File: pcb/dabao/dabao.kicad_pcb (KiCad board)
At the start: 2 copper layers, 127.4 x 114.6 mm, 74 parts, among them J1 Conn_01x05, J2 USB_C_Receptacle_USB2.0_16P, J3 Conn_01x04, J4 MagConn_01x04_Pin, J5 Conn_Battery, J7 Conn_01x04, J8 Display, SW1 SW_RESET, SW2 SW_POWER, U1 nice_nano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

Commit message: Add nets, tweak layout
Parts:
- moved REF** 4.97 mm to (168.5, 79.5)
- moved S3 4.45 mm to (104.5, 71.9)
- moved C1 4.45 mm to (135.7, 105.0)
- moved D2 4.45 mm to (102.7, 84.9)
- moved D3 4.45 mm to (107.1, 68.5)
- moved J8 4.45 mm to (206.8, 105.2)
- moved JP6 4.45 mm to (204.3, 123.7)
- moved JP8 4.45 mm to (204.3, 123.7)
- moved S18 4.45 mm to (184.3, 141.9)
- moved S8 4.45 mm to (141.1, 78.1)
- moved S12 4.45 mm to (162.3, 68.8)
- moved S7 4.45 mm to (136.7, 94.6)
- moved D13 4.45 mm to (172.8, 105.4)
- moved REF** 4.45 mm to (188.4, 128.5)
- moved S16 4.45 mm to (149.9, 122.0)
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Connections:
- J2 pad S1: unconnected-(J2-SHIELD-PadS1) -> GND
- U1 pad 29: unconnected-(U1-BAT+-Pad29) -> /BAT+
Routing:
- net /col_ring: track 180.7 -> 181.9 mm
- net /col_pinky: track 199.1 -> 199.9 mm
- net GND: vias 70 -> 73

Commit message: Add logo, update library path
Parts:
- added G***: LOGO, Library:takeout-text, F.Cu at (201.6, 142.7)
- added G***: LOGO, Library:takeout-logo, B.Cu at (200.0, 138.8)
- moved C1 2.22 mm to (134.9, 102.9)
- moved S15 2.22 mm to (178.1, 73.9)
- moved REF** 2.22 mm to (109.8, 82.4)
- moved S1 2.22 mm to (94.9, 102.6)
- moved S3 2.22 mm to (103.7, 69.8)
- moved D11 2.22 mm to (159.4, 79.8)
- moved J5 2.22 mm to (203.9, 110.2)
- moved JP3 2.22 mm to (208.4, 118.9)
- moved S12 2.22 mm to (161.4, 66.8)
- moved S17 2.22 mm to (167.6, 127.7)
- moved JP2 2.22 mm to (208.5, 121.7)
- moved JP5 2.22 mm to (203.5, 118.9)
- moved JP7 2.22 mm to (203.4, 118.9)
- moved R4 2.22 mm to (196.1, 88.2)
- moved REF** 2.22 mm to (167.6, 77.5)
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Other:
- board text added: "v1.0"
- board text removed: "打包 v1.0"

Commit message: Updates to models
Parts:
- moved REF** 20.6 mm to (188.1, 79.5)
- moved REF** 14.4 mm to (122.9, 49.0)
- moved REF** 2.29 mm to (188.6, 124.5)
- moved REF** 2.22 mm to (198.4, 151.9)
- moved D13 2.22 mm to (171.1, 101.3)
- moved D7 2.22 mm to (137.6, 87.1)
- moved JP11 2.22 mm to (198.1, 96.3)
- moved R8 2.22 mm to (130.3, 99.9)
- moved S16 2.22 mm to (148.2, 117.9)
- moved S17 2.22 mm to (166.7, 125.6)
- moved U2 2.22 mm to (185.9, 108.4)
- moved S1 2.22 mm to (94.0, 100.6)
- moved J7 2.22 mm to (197.7, 125.3)
- moved JP2 2.22 mm to (207.6, 119.6)
- moved JP5 2.22 mm to (202.6, 116.9)
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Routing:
- net GND: track 67.0 -> 64.6 mm, vias 73 -> 74
- net Net-(J5-Pin_2): track 115.3 -> 114.0 mm
- net /BAT+: track 68.7 -> 67.4 mm

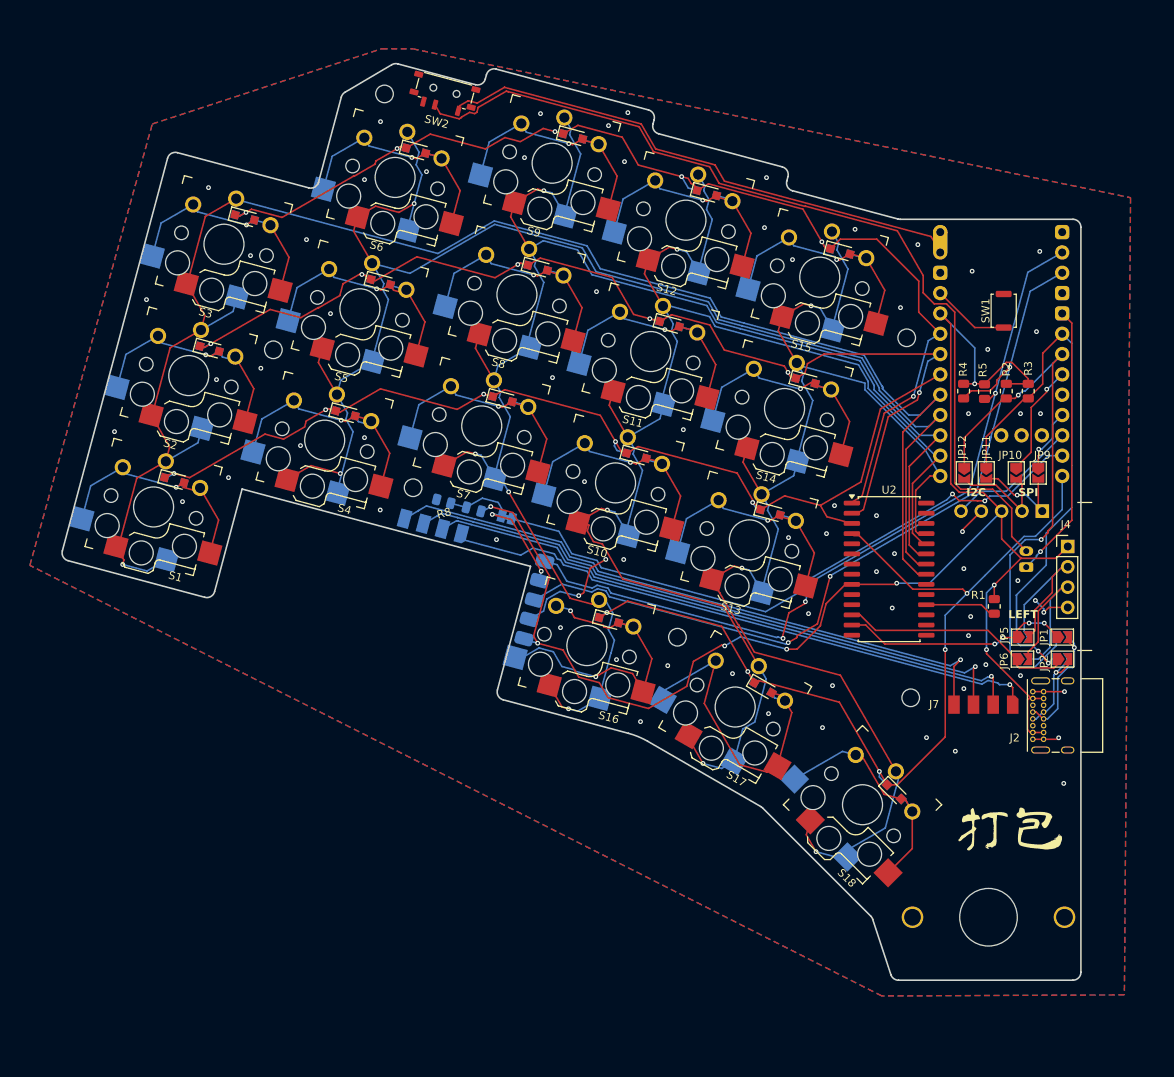
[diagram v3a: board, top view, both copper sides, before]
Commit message: PCB updates to fix assembly issues
Addresses https://github.com/justinmklam/dabao/issues/1
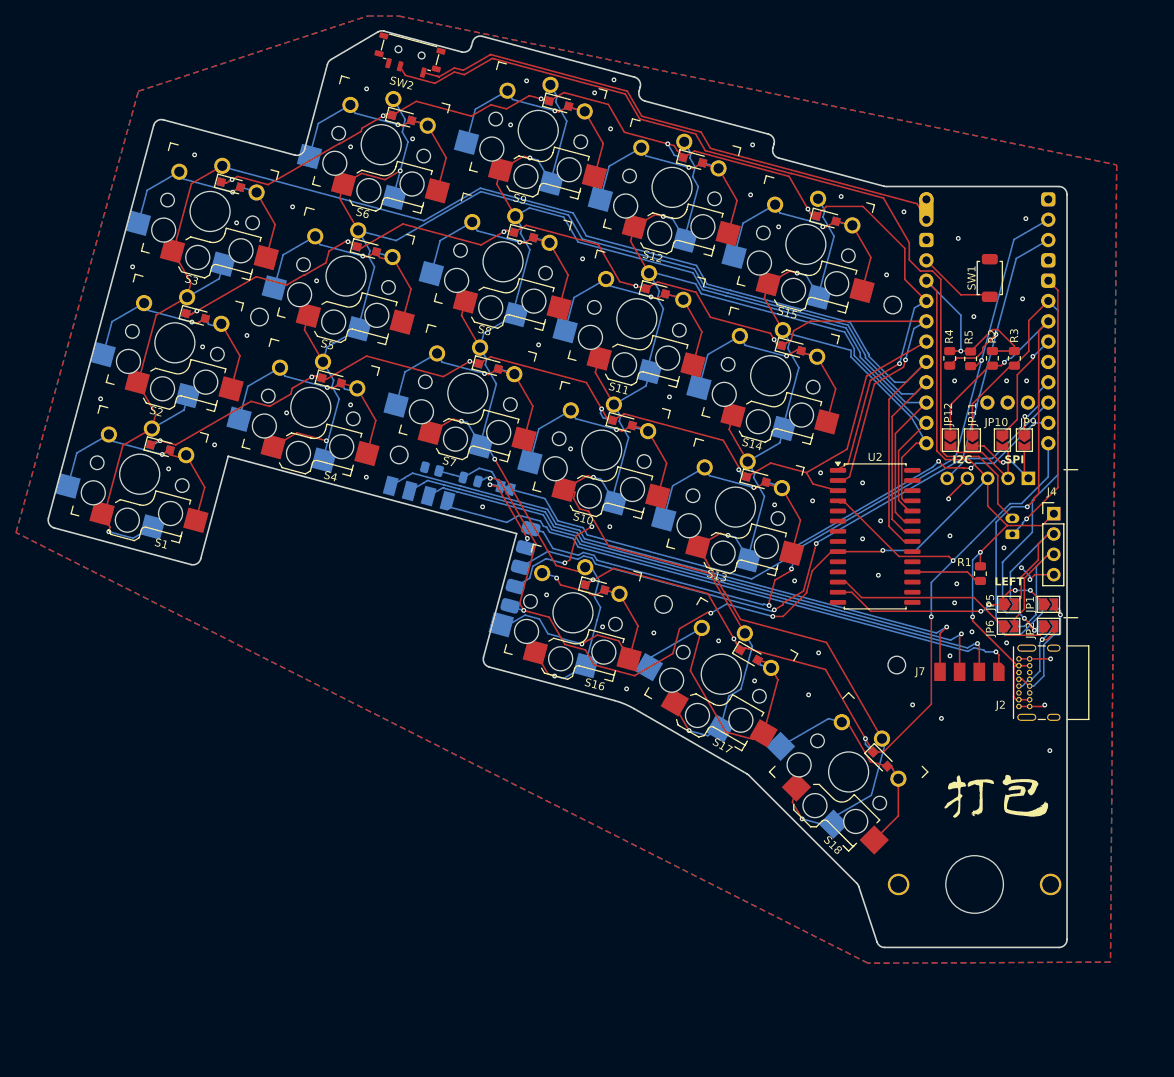
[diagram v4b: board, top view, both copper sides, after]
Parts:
- removed the REF** at (122.9, 49.0)
- moved SW2 6.49 mm to (126.0, 43.8)
- moved J2 4.45 mm to (202.2, 125.5)
- moved J7 4.45 mm to (196.0, 121.2)
- moved JP5 4.45 mm to (200.9, 112.8)
- moved S14 4.45 mm to (171.1, 84.2)
- moved D1 4.45 mm to (94.8, 93.2)
- moved JP11 4.45 mm to (196.3, 92.2)
- moved JP2 4.45 mm to (205.9, 115.5)
- moved REF** 4.45 mm to (196.6, 147.8)
- moved S6 4.45 mm to (122.4, 55.3)
- moved U1 4.45 mm to (198.2, 78.7)
- moved D12 4.45 mm to (161.4, 57.3)
- moved D5 4.45 mm to (120.6, 68.4)
- moved D7 4.45 mm to (135.9, 83.0)
- moved R4 4.45 mm to (193.5, 82.0)
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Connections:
- U2 pad 15: unconnected-(U2-A0-Pad15) -> GND
- U2 pad 16: unconnected-(U2-A1-Pad16) -> GND
- U2 pad 17: unconnected-(U2-A2-Pad17) -> GND
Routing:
- net /BAT+: track 67.4 -> 70.1 mm
- net Net-(J5-Pin_2): track 114.0 -> 116.4 mm
- net /TP_reset: track 78.9 -> 76.9 mm
- net VDD: track 196.4 -> 195.0 mm
- net Net-(J1-Pin_2): track 21.1 -> 20.6 mm
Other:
- board text added: "jmklam v1.0"
- board text removed: "v1.0"
